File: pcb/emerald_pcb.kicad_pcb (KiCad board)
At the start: 2 copper layers, 74.8 x 53.9 mm, 37 parts, among them J1 SIM_Card, J2 USB_B_Mini, SW1 ESP RESET, U1 ESP32-S3-MINI-1U, U2 SIM800C, U3 SX1278, U4 MPU-6050, U5 FXMA108, U6 CH340N, U7 PTN78000W_EUS-5, U8 AMS1117-3.3

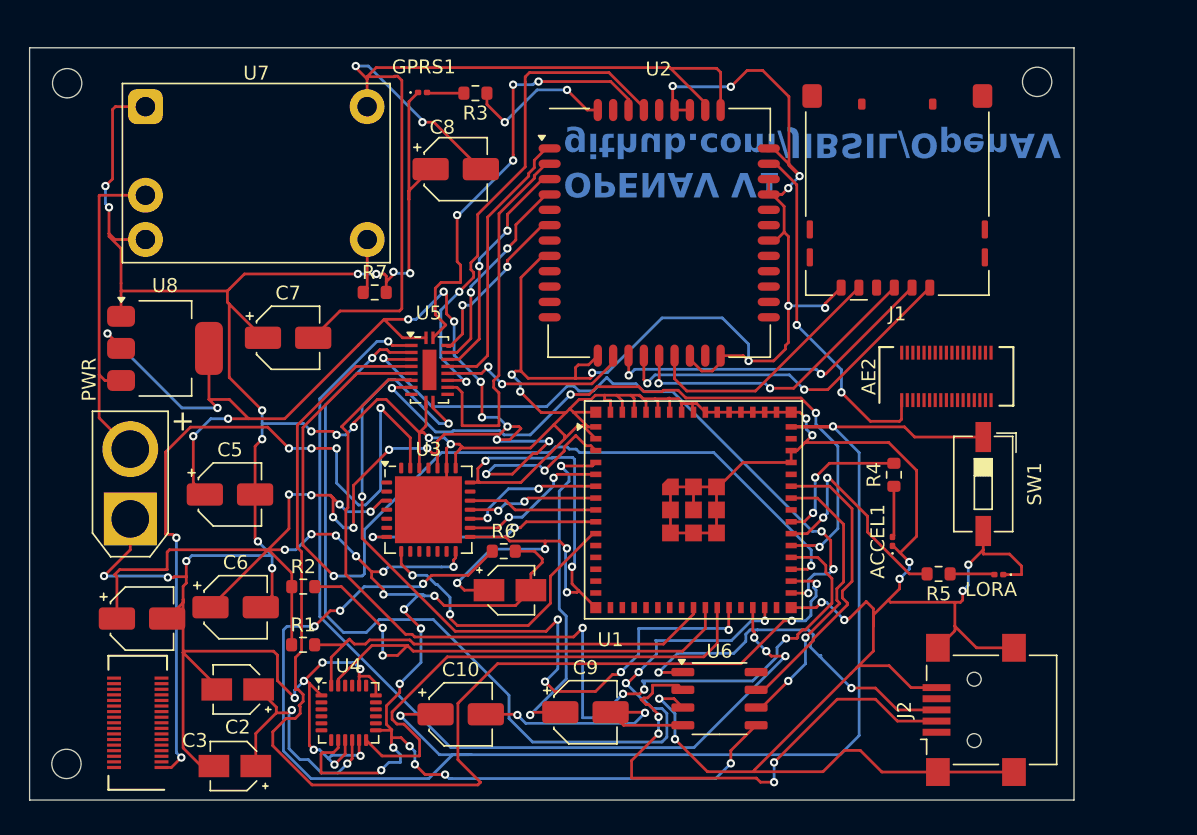
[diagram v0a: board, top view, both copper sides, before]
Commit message: feat: update to version 1.1
Changed power inputs, various schematic changes, added decoupling capacitors, removed rare components
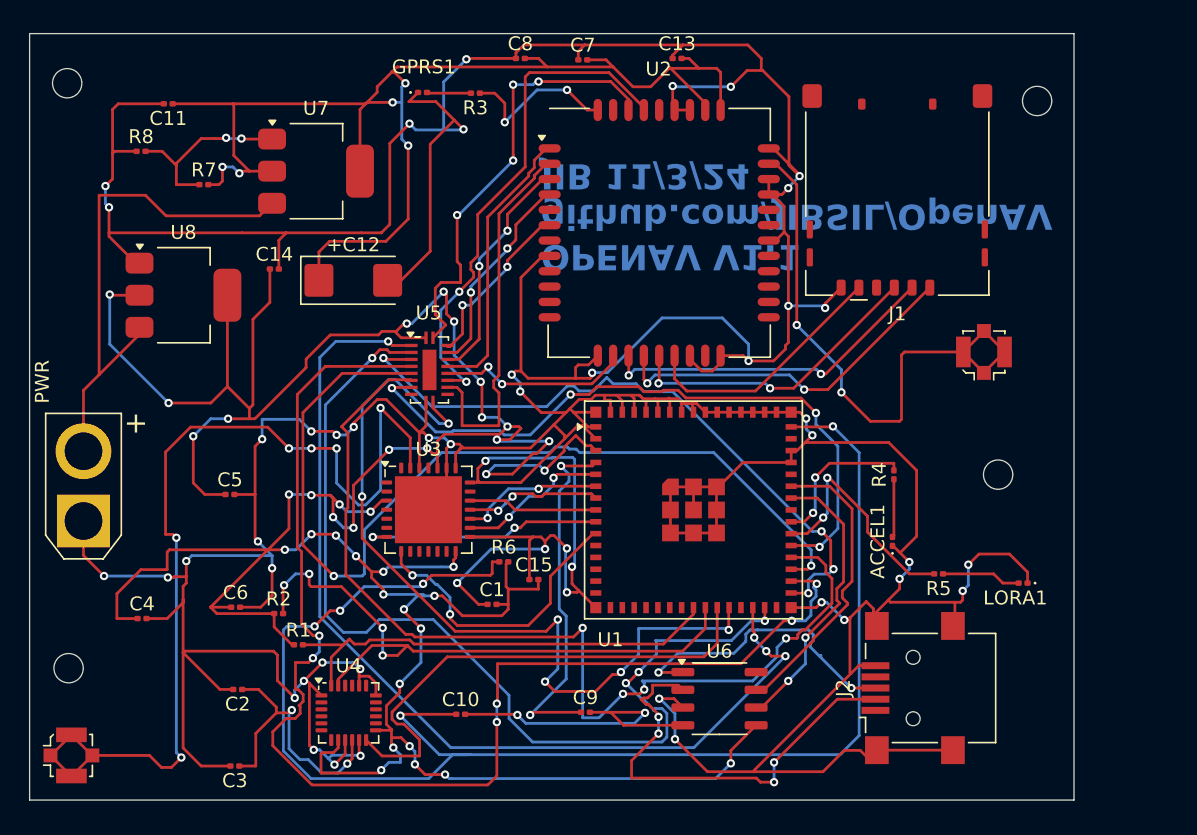
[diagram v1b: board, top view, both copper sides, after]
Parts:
- removed AE1: LoRaAntenna, Connector:GB042-34S-H10
- removed AE2: GSMAntenna, Connector:GB042-34S-H10
- removed SW1: ESP RESET, Button_Switch_SMD:SW_DIP_SPSTx01_Slide_6.7x4.1mm_W6.73mm_P2.54mm_LowProfile_JPin
- added +C12: 100uF TANT, Capacitor_Tantalum_SMD:CP_EIA-6032-15_Kemet-U, F.Cu at (57.9, 52.2)
- added C11: 22uF, Capacitor_SMD:C_0201_0603Metric, F.Cu at (44.7, 39.6)
- added C13: 10pF, Capacitor_SMD:C_0201_0603Metric, F.Cu at (81.1, 36.3)
- added C14: 22uF, Capacitor_SMD:C_0201_0603Metric, F.Cu at (52.3, 51.4)
- added C15: 22uF, Capacitor_SMD:C_0201_0603Metric, F.Cu at (70.9, 73.7)
- added R8: 2K, Resistor_SMD:R_0201_0603Metric, F.Cu at (42.7, 43.0)
- added REF**: GSMConn, Connector_Coaxial:U.FL_Molex_MCRF_73412-0110_Vertical, F.Cu at (103.1, 57.4)
- added REF**: MountingHole_2.1mm, MountingHole:MountingHole_2.1mm, F.Cu at (104.1, 66.1)
- added REF**: LoRaAnt, Connector_Coaxial:U.FL_Molex_MCRF_73412-0110_Vertical, F.Cu at (37.7, 86.3)
- C1, C2: value 0.1uF -> 0.1uF X7R 4V; footprint Capacitor_SMD:CP_Elec_3x5.3 -> Capacitor_SMD:C_0201_0603Metric
- C10, C4, C5, C6, C9: footprint Capacitor_SMD:CP_Elec_4x3 -> Capacitor_SMD:C_0201_0603Metric
- C3: value 2.2nF -> 2.2nF X7R 50V; footprint Capacitor_SMD:CP_Elec_3x5.3 -> Capacitor_SMD:C_0201_0603Metric
- C7: value 300uF -> 1uF; footprint Capacitor_SMD:CP_Elec_4x3 -> Capacitor_SMD:C_0201_0603Metric
- C8: value 300uF -> 33pF; footprint Capacitor_SMD:CP_Elec_4x3 -> Capacitor_SMD:C_0201_0603Metric
- R1, R2, R3, R4, R5, R6: footprint Resistor_SMD:R_0603_1608Metric -> Resistor_SMD:R_0201_0603Metric
- R7: value 36.4k -> 1K; footprint Resistor_SMD:R_0603_1608Metric -> Resistor_SMD:R_0201_0603Metric
- U7: value PTN78000W_EUS-5 -> AMS1117; footprint Module:Texas_EUS_R-PDSS-T5_THT -> Package_TO_SOT_SMD:SOT-223-3_TabPin2
- moved C7 29.0 mm to (74.4, 36.4)
- moved R7 14.5 mm to (47.2, 45.4)
- moved U7 13.1 mm to (55.3, 44.4)
- moved C8 9.19 mm to (69.9, 36.3)
- moved REF** 6.86 mm to (37.5, 80.0)
- moved J2 4.65 mm to (98.1, 81.4)
- moved U8 4.03 mm to (45.8, 53.3)
- moved PWR 3.36 mm to (38.6, 69.5)
- moved R2 2.62 mm to (52.6, 76.1)
- moved LORA1 1.84 mm to (105.9, 73.9)
- moved C1 1.64 mm to (67.9, 75.4)
- moved REF** 1.37 mm to (106.9, 39.4)
- moved R6 0.76 mm to (68.7, 72.4)
- moved R1 0.33 mm to (54.0, 78.3)
- renumbered LORA to LORA1
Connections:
- ACCEL1 pad 1: GND -> Net-(ACCEL1-K)
- C1 pad 1: GND -> Net-(ACCEL1-K)
- C2 pad 2: GND -> Net-(ACCEL1-K)
- C3 pad 2: GND -> Net-(ACCEL1-K)
- C4 pad 2: GND -> Net-(ACCEL1-K)
- C5 pad 2: GND -> Net-(ACCEL1-K)
- C6 pad 2: GND -> Net-(ACCEL1-K)
- C7 pad 1: GND -> Net-(ACCEL1-K)
- C8 pad 1: GND -> Net-(ACCEL1-K)
- GPRS1 pad 1: GND -> Net-(ACCEL1-K)
- J1 pad 5: GND -> Net-(ACCEL1-K)
- J2 pad 5: GND -> Net-(ACCEL1-K)
- J2 pad 6: GND -> Net-(ACCEL1-K)
- LORA1 pad 1: GND -> Net-(ACCEL1-K)
- PWR pad 1: GND -> Net-(ACCEL1-K)
- R7 pad 1: Net-(U7-Vo_Adj) -> Net-(U7-ADJ)
- R7 pad 2: GND -> Net-(U7-VO)
- U1 pad 1: GND -> Net-(ACCEL1-K)
- U1 pad 2: GND -> Net-(ACCEL1-K)
- U1 pad 42: GND -> Net-(ACCEL1-K)
- U1 pad 43: GND -> Net-(ACCEL1-K)
- U1 pad 46: GND -> Net-(ACCEL1-K)
- U1 pad 47: GND -> Net-(ACCEL1-K)
- U1 pad 48: GND -> Net-(ACCEL1-K)
- U1 pad 49: GND -> Net-(ACCEL1-K)
- U1 pad 50: GND -> Net-(ACCEL1-K)
- U1 pad 51: GND -> Net-(ACCEL1-K)
- U1 pad 52: GND -> Net-(ACCEL1-K)
- U1 pad 53: GND -> Net-(ACCEL1-K)
- U1 pad 54: GND -> Net-(ACCEL1-K)
- U1 pad 55: GND -> Net-(ACCEL1-K)
- U1 pad 56: GND -> Net-(ACCEL1-K)
- U1 pad 57: GND -> Net-(ACCEL1-K)
- U1 pad 58: GND -> Net-(ACCEL1-K)
- U1 pad 59: GND -> Net-(ACCEL1-K)
- U1 pad 60: GND -> Net-(ACCEL1-K)
- U1 pad 61: GND -> Net-(ACCEL1-K)
- U1 pad 62: GND -> Net-(ACCEL1-K)
- U1 pad 63: GND -> Net-(ACCEL1-K)
- U1 pad 64: GND -> Net-(ACCEL1-K)
- U1 pad 65: GND -> Net-(ACCEL1-K)
- U2 pad 13: GND -> Net-(ACCEL1-K)
- U2 pad 19: GND -> Net-(ACCEL1-K)
- U2 pad 21: GND -> Net-(ACCEL1-K)
- U2 pad 27: GND -> Net-(ACCEL1-K)
- U2 pad 30: GND -> Net-(ACCEL1-K)
- U2 pad 31: GND -> Net-(ACCEL1-K)
- U2 pad 33: GND -> Net-(ACCEL1-K)
- U2 pad 36: GND -> Net-(ACCEL1-K)
- U2 pad 37: GND -> Net-(ACCEL1-K)
- U2 pad 8: GND -> Net-(ACCEL1-K)
- U3 pad 15: GND -> Net-(ACCEL1-K)
- U3 pad 21: GND -> Net-(ACCEL1-K)
- U3 pad 22: GND -> Net-(ACCEL1-K)
- U3 pad 23: GND -> Net-(ACCEL1-K)
- U3 pad 26: GND -> Net-(ACCEL1-K)
- U3 pad 29: GND -> Net-(ACCEL1-K)
- U4 pad 1: GND -> Net-(ACCEL1-K)
- U4 pad 11: GND -> Net-(ACCEL1-K)
- U4 pad 18: GND -> Net-(ACCEL1-K)
- U4 pad 20: GND -> Net-(ACCEL1-K)
- U4 pad 9: GND -> Net-(ACCEL1-K)
- U5 pad 10: GND -> Net-(ACCEL1-K)
- U6 pad 3: GND -> Net-(ACCEL1-K)
- U7 pad 1: GND -> Net-(U7-ADJ)
- U7 pad 2: Net-(J3-Pin_1) -> Net-(U7-VO)
- U7 pad 3: GND -> Net-(J3-Pin_1)
- U8 pad 1: GND -> Net-(ACCEL1-K)
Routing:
- net Net-(ACCEL1-K): track 0.00 -> 532.2 mm, vias 0 -> 49
- net GND: track 509.1 -> 0.00 mm, vias 51 -> 0
- net Net-(U1-3V3): track 236.5 -> 257.1 mm
- net Net-(U7-VO): track 74.3 -> 93.9 mm, vias 2 -> 5
- net Net-(AE2-A): track 25.4 -> 41.6 mm
- net Net-(AE1-A): track 55.8 -> 69.6 mm
- net Net-(U7-ADJ): track 0.00 -> 13.5 mm, vias 0 -> 2
- net Net-(J3-Pin_1): track 24.2 -> 36.8 mm
- net Net-(U1-EN): track 117.9 -> 106.0 mm
- net Net-(U1-IO20): track 40.2 -> 45.7 mm, vias 2 -> 4
- net Net-(J2-D-): track 36.8 -> 31.8 mm
- net Net-(J2-D+): track 26.6 -> 21.6 mm
- net Net-(U7-Vo_Adj): track 3.91 -> 0.00 mm
- net Net-(U6-~{RTS}): track 20.0 -> 23.0 mm
- net Net-(LORA1-A): track 3.19 -> 5.69 mm
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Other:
- board size 74.8 x 53.9 mm -> 74.8 x 54.9 mm
- board text added: "OPENAV V1.1 github.com/JIBSIL/OpenAV JIB 11/3/24"
- board text removed: "OPENAV V1 github.com/JIBSIL/OpenAV"

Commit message: feat: added pins to schem. fix: D+ and D- pins being assigned on ESP32
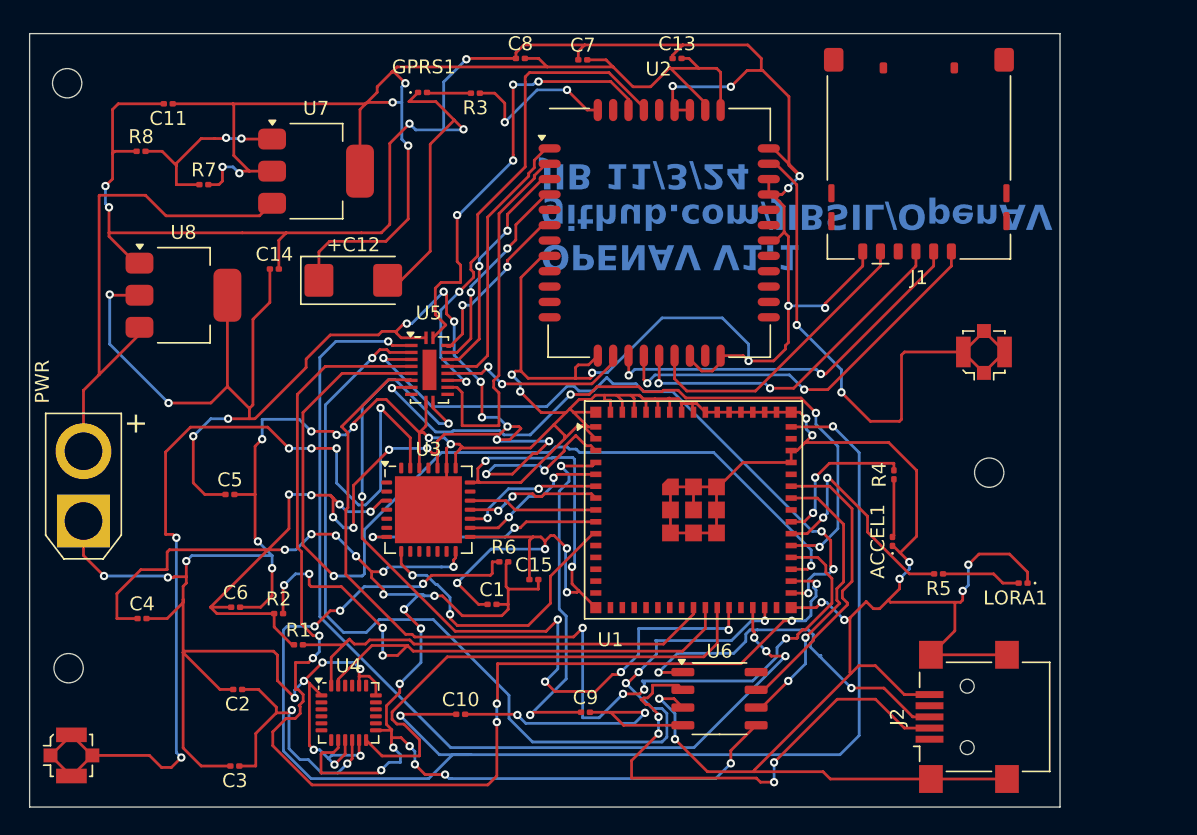
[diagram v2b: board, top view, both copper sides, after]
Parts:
- removed the REF** at (106.9, 39.4)
- moved J2 4.39 mm to (101.9, 83.5)
- moved J1 3.02 mm to (98.5, 43.5)
- moved REF** 0.66 mm to (103.5, 66.0)
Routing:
- net Net-(ACCEL1-K): track 532.2 -> 548.7 mm
- net Net-(J2-D-): track 31.8 -> 36.6 mm
- net Net-(J2-D+): track 21.6 -> 26.3 mm
- net Net-(J1-RST): track 22.0 -> 25.3 mm
- net Net-(J1-I/O): track 24.6 -> 27.8 mm
- net Net-(J1-CLK): track 26.1 -> 29.3 mm
- net Net-(J1-VCC): track 18.3 -> 21.5 mm
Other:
- board size 74.8 x 54.9 mm -> 73.8 x 55.4 mm

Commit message: feat: reroute for fewer vias, simplify design
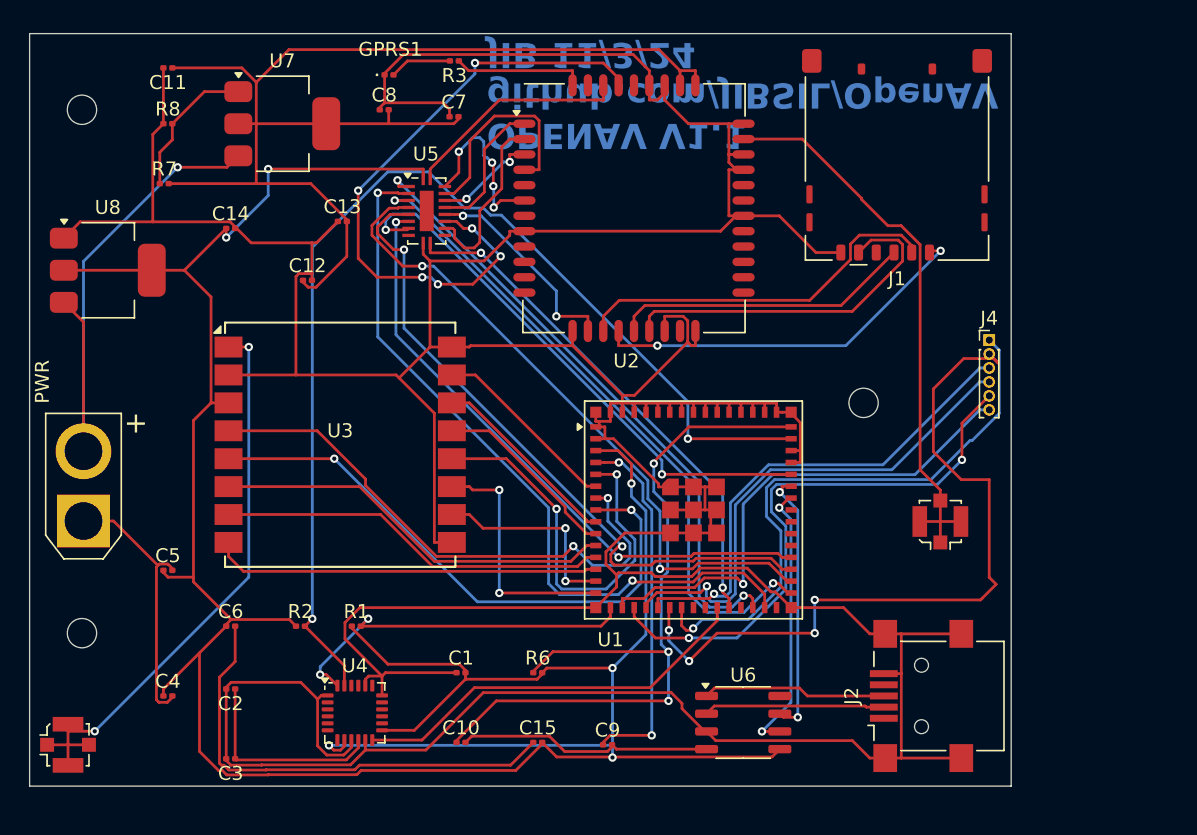
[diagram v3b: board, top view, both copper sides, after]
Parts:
- removed ACCEL1, LORA1: LED, LED_SMD:LED_0201_0603Metric
- removed R4, R5: 1K, Resistor_SMD:R_0201_0603Metric
- added J4: Extra Connectors, Connector_PinHeader_1.00mm:PinHeader_1x06_P1.00mm_Vertical, F.Cu at (103.5, 56.5)
- C1, C2: value 0.1uF X7R 4V -> 0.1uF
- C12: renamed from +C12; footprint Capacitor_Tantalum_SMD:CP_EIA-6032-15_Kemet-U -> Capacitor_SMD:C_0201_0603Metric
- C3: value 2.2nF X7R 50V -> 2.2nF
- U3: value SX1278 -> Ra-01; footprint Package_DFN_QFN:QFN-28-1EP_6x6mm_P0.65mm_EP4.8x4.8mm -> RF_Module:Ai-Thinker-Ra-01-LoRa
- moved C13 26.7 mm to (57.2, 48.0)
- moved ANT2 12.5 mm to (100.0, 69.5)
- moved C15 11.7 mm to (71.2, 85.3)
- moved U5 11.4 mm to (63.2, 47.2)
- moved C8 10.4 mm to (60.2, 40.0)
- moved S1 10.3 mm to (94.5, 61.0)
- moved C7 10.1 mm to (65.2, 40.5)
- moved R6 8.31 mm to (71.2, 80.3)
- moved U3 7.85 mm to (57.0, 64.0)
- moved C5 7.02 mm to (44.7, 73.0)
- moved C4 5.85 mm to (44.7, 82.0)
- moved U8 5.71 mm to (40.4, 51.5)
- moved C1 5.38 mm to (65.7, 80.3)
- moved R1 4.35 mm to (58.2, 77.0)
- moved C14 4.27 mm to (49.2, 48.5)
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- renumbered REF** to ANT1, REF** to ANT2, REF** to S1, REF** to S2, REF** to S3
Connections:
- C1 pad 1: Net-(ACCEL1-K) -> Net-(GPRS1-K)
- C11 pad 2: Net-(ACCEL1-K) -> Net-(GPRS1-K)
- C12 pad 2: Net-(ACCEL1-K) -> Net-(GPRS1-K)
- C13 pad 1: Net-(ACCEL1-K) -> Net-(GPRS1-K)
- C14 pad 2: Net-(ACCEL1-K) -> Net-(GPRS1-K)
- C15 pad 1: Net-(ACCEL1-K) -> Net-(C15-Pad1)
- C2 pad 2: Net-(ACCEL1-K) -> Net-(GPRS1-K)
- C3 pad 2: Net-(ACCEL1-K) -> Net-(GPRS1-K)
- C6 pad 2: Net-(ACCEL1-K) -> Net-(C15-Pad1)
- C7 pad 1: Net-(ACCEL1-K) -> Net-(GPRS1-K)
- C8 pad 1: Net-(ACCEL1-K) -> Net-(GPRS1-K)
- GPRS1 pad 1: Net-(ACCEL1-K) -> Net-(GPRS1-K)
- J1 pad 5: Net-(ACCEL1-K) -> Net-(GPRS1-K)
- J2 pad 5: Net-(ACCEL1-K) -> Net-(GPRS1-K)
- J2 pad 6: Net-(ACCEL1-K) -> Net-(GPRS1-K)
- R1 pad 2: Net-(U1-IO19) -> Net-(U1-IO12)
- R2 pad 2: Net-(U1-IO20) -> Net-(U1-IO46)
- R8 pad 1: Net-(ACCEL1-K) -> Net-(GPRS1-K)
- U1 pad 1: Net-(ACCEL1-K) -> Net-(GPRS1-K)
- U1 pad 11: unconnected-(U1-IO7-Pad11) -> Net-(U1-IO7)
- U1 pad 12: unconnected-(U1-IO8-Pad12) -> Net-(U1-IO8)
- U1 pad 13: unconnected-(U1-IO9-Pad13) -> Net-(U1-IO9)
- U1 pad 14: unconnected-(U1-IO10-Pad14) -> Net-(U1-IO10)
- U1 pad 15: unconnected-(U1-IO11-Pad15) -> Net-(U1-IO11)
- U1 pad 16: unconnected-(U1-IO12-Pad16) -> Net-(U1-IO12)
- U1 pad 17: unconnected-(U1-IO13-Pad17) -> Net-(J4-Pin_6)
- U1 pad 18: unconnected-(U1-IO14-Pad18) -> Net-(J4-Pin_5)
- U1 pad 19: unconnected-(U1-IO15-Pad19) -> Net-(J4-Pin_4)
- U1 pad 2: Net-(ACCEL1-K) -> Net-(GPRS1-K)
- U1 pad 20: unconnected-(U1-IO16-Pad20) -> Net-(J4-Pin_3)
- U1 pad 21: unconnected-(U1-IO17-Pad21) -> Net-(J4-Pin_2)
- U1 pad 22: unconnected-(U1-IO18-Pad22) -> Net-(J4-Pin_1)
- U1 pad 23: Net-(U1-IO19) -> unconnected-(U1-IO19-Pad23)
- U1 pad 24: Net-(U1-IO20) -> unconnected-(U1-IO20-Pad24)
- U1 pad 35: Net-(U1-IO39) -> unconnected-(U1-IO39-Pad35)
- U1 pad 36: Net-(U1-IO40) -> unconnected-(U1-IO40-Pad36)
- U1 pad 37: Net-(U1-IO41) -> unconnected-(U1-IO41-Pad37)
- U1 pad 41: unconnected-(U1-IO45-Pad41) -> Net-(U1-IO45)
- U1 pad 42: Net-(ACCEL1-K) -> Net-(GPRS1-K)
- U1 pad 43: Net-(ACCEL1-K) -> Net-(GPRS1-K)
- U1 pad 44: unconnected-(U1-IO46-Pad44) -> Net-(U1-IO46)
- U1 pad 46: Net-(ACCEL1-K) -> Net-(GPRS1-K)
- U1 pad 47: Net-(ACCEL1-K) -> Net-(GPRS1-K)
- U1 pad 48: Net-(ACCEL1-K) -> Net-(GPRS1-K)
- U1 pad 49: Net-(ACCEL1-K) -> Net-(GPRS1-K)
- U1 pad 50: Net-(ACCEL1-K) -> Net-(GPRS1-K)
- U1 pad 51: Net-(ACCEL1-K) -> Net-(GPRS1-K)
- U1 pad 52: Net-(ACCEL1-K) -> Net-(GPRS1-K)
- U1 pad 53: Net-(ACCEL1-K) -> Net-(GPRS1-K)
- U1 pad 54: Net-(ACCEL1-K) -> Net-(GPRS1-K)
- U1 pad 55: Net-(ACCEL1-K) -> Net-(GPRS1-K)
- U1 pad 56: Net-(ACCEL1-K) -> Net-(GPRS1-K)
- U1 pad 57: Net-(ACCEL1-K) -> Net-(GPRS1-K)
- U1 pad 58: Net-(ACCEL1-K) -> Net-(GPRS1-K)
- U1 pad 59: Net-(ACCEL1-K) -> Net-(GPRS1-K)
- U1 pad 60: Net-(ACCEL1-K) -> Net-(GPRS1-K)
- U1 pad 61: Net-(ACCEL1-K) -> Net-(GPRS1-K)
- U1 pad 62: Net-(ACCEL1-K) -> Net-(GPRS1-K)
- U1 pad 63: Net-(ACCEL1-K) -> Net-(GPRS1-K)
- U1 pad 64: Net-(ACCEL1-K) -> Net-(GPRS1-K)
- U1 pad 65: Net-(ACCEL1-K) -> Net-(GPRS1-K)
- U2 pad 13: Net-(ACCEL1-K) -> Net-(GPRS1-K)
- U2 pad 19: Net-(ACCEL1-K) -> Net-(GPRS1-K)
- U2 pad 21: Net-(ACCEL1-K) -> Net-(GPRS1-K)
- U2 pad 27: Net-(ACCEL1-K) -> Net-(GPRS1-K)
- U2 pad 30: Net-(ACCEL1-K) -> Net-(GPRS1-K)
- U2 pad 31: Net-(ACCEL1-K) -> Net-(GPRS1-K)
- U2 pad 33: Net-(ACCEL1-K) -> Net-(GPRS1-K)
- U2 pad 36: Net-(ACCEL1-K) -> Net-(GPRS1-K)
- U2 pad 37: Net-(ACCEL1-K) -> Net-(GPRS1-K)
- U2 pad 8: Net-(ACCEL1-K) -> Net-(GPRS1-K)
- U3 pad 1: unconnected-(U3-RFI_LF-Pad1) -> Net-(AE1-A)
- U3 pad 10: unconnected-(U3-DIO2-Pad10) -> Net-(U1-IO10)
- U3 pad 11: unconnected-(U3-DIO3-Pad11) -> Net-(U1-IO11)
- U3 pad 12: unconnected-(U3-DIO4-Pad12) -> Net-(U1-IO1)
- U3 pad 13: unconnected-(U3-DIO5-Pad13) -> Net-(U1-IO6)
- U3 pad 14: Net-(U1-3V3) -> Net-(U1-IO5)
- U3 pad 15: Net-(ACCEL1-K) -> Net-(U1-IO2)
- U3 pad 16: Net-(U1-IO1) -> Net-(GPRS1-K)
- U3 pad 2: unconnected-(U3-VR_ANA-Pad2) -> Net-(GPRS1-K)
- U3 pad 4: unconnected-(U3-VR_DIG-Pad4) -> Net-(U1-IO3)
- U3 pad 5: unconnected-(U3-XTA-Pad5) -> Net-(U1-IO4)
- U3 pad 6: unconnected-(U3-XTB-Pad6) -> Net-(U1-IO7)
- U3 pad 7: Net-(U1-IO5) -> Net-(U1-IO8)
- U3 pad 8: Net-(U1-IO6) -> Net-(U1-IO9)
- U3 pad 9: unconnected-(U3-DIO1-Pad9) -> Net-(GPRS1-K)
- U4 pad 1: Net-(ACCEL1-K) -> Net-(GPRS1-K)
- U4 pad 11: Net-(ACCEL1-K) -> Net-(GPRS1-K)
- U4 pad 18: Net-(ACCEL1-K) -> Net-(GPRS1-K)
- U4 pad 20: Net-(ACCEL1-K) -> Net-(GPRS1-K)
- U4 pad 23: Net-(U1-IO20) -> Net-(U1-IO46)
- U4 pad 24: Net-(U1-IO19) -> Net-(U1-IO12)
- U4 pad 9: Net-(ACCEL1-K) -> Net-(GPRS1-K)
- U5 pad 10: Net-(ACCEL1-K) -> Net-(GPRS1-K)
- U5 pad 8: Net-(U1-IO39) -> Net-(U1-IO45)
- U6 pad 3: Net-(ACCEL1-K) -> Net-(GPRS1-K)
- U8 pad 1: Net-(ACCEL1-K) -> Net-(GPRS1-K)
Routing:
- net Net-(ACCEL1-K): track 548.7 -> 19.1 mm, vias 49 -> 0
- net Net-(GPRS1-K): track 0.00 -> 400.2 mm
- net Net-(U1-IO46): track 0.00 -> 78.8 mm, vias 0 -> 2
- net Net-(U1-3V3): track 257.1 -> 202.1 mm, vias 39 -> 6
- net Net-(J4-Pin_2): track 0.00 -> 53.8 mm, vias 0 -> 4
- net Net-(U1-EN): track 106.0 -> 55.7 mm, vias 5 -> 3
- net Net-(U1-IO39): track 48.4 -> 0.00 mm, vias 4 -> 0
- net Net-(U1-IO20): track 45.7 -> 0.00 mm, vias 4 -> 0
- net Net-(U1-IO36): track 92.2 -> 47.7 mm, vias 6 -> 2
- net Net-(J4-Pin_1): track 0.00 -> 41.8 mm, vias 0 -> 1
- net Net-(J4-Pin_5): track 0.00 -> 41.1 mm, vias 0 -> 2
- net Net-(U1-IO45): track 0.00 -> 39.9 mm, vias 0 -> 2
- net Net-(J4-Pin_4): track 0.00 -> 36.6 mm, vias 0 -> 1
- net Net-(J4-Pin_6): track 0.00 -> 36.3 mm, vias 0 -> 1
- net Net-(J4-Pin_3): track 0.00 -> 35.1 mm, vias 0 -> 1
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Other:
- board size 73.8 x 55.4 mm -> 70.3 x 53.9 mm
